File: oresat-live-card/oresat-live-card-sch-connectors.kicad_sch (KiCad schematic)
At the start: 14 parts, among them J1 ORESAT-DEBUG-CONNECTOR, J4 TFM-120-01-L-D-RA, J6 SMPM, J8 SMPM

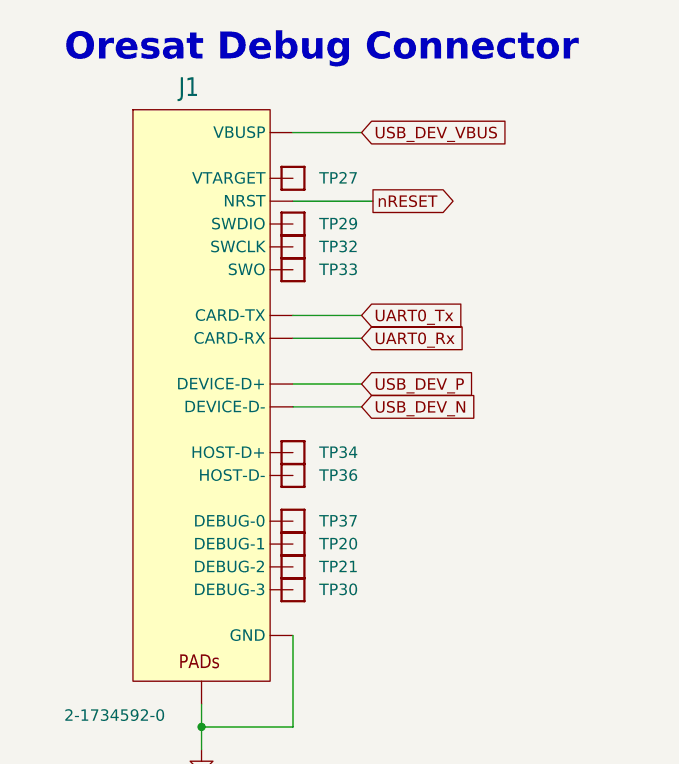
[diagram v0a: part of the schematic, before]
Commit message: Updated OPD / power page and synced with CFC processor, fixed layout issues.
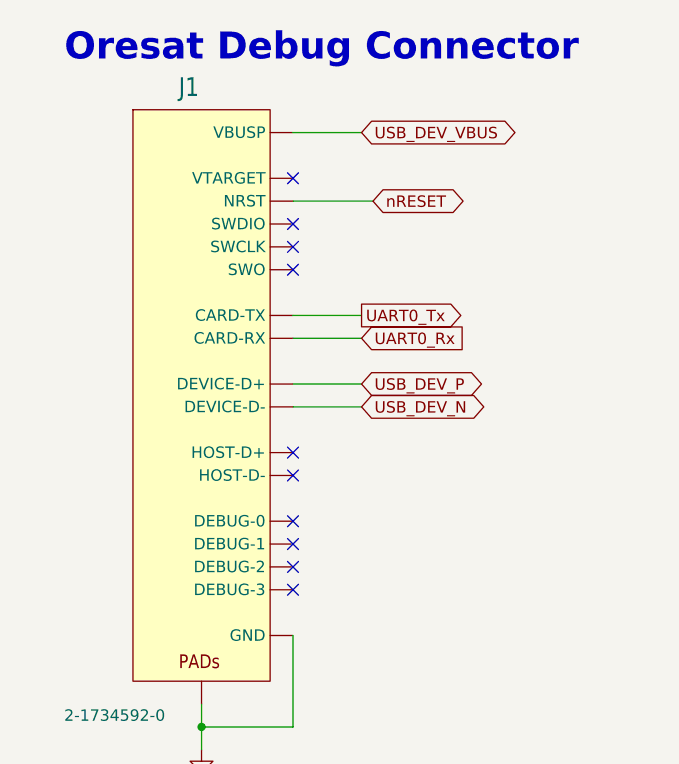
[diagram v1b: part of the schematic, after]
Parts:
- removed TP20, TP21, TP27, TP29, TP30, TP32, TP33, TP34, TP36, TP37: TEST-POINT, oresat-misc:TestPoint_Pad_D1.0mm, symbol oresat-misc:Test-Point-1mm-round
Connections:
- no-connect marks 20 -> 30

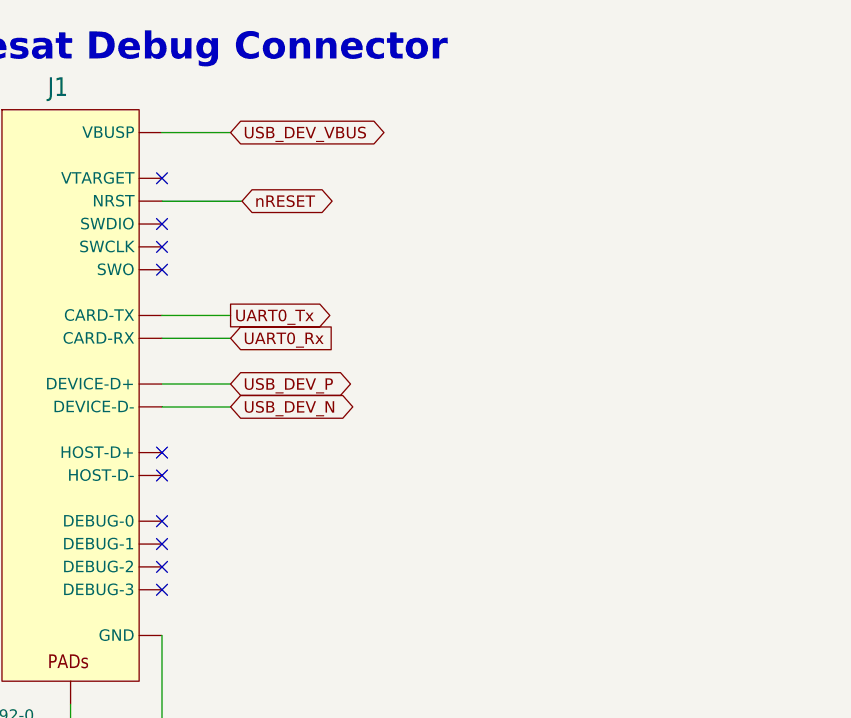
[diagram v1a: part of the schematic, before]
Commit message: Updated SIP A, B, and C. Lots of cleanup of crazy routing - this board is long in the tooth and has been rerouted several times, so there's a lot of crazy routing. Cleaning up a bit is really helping.
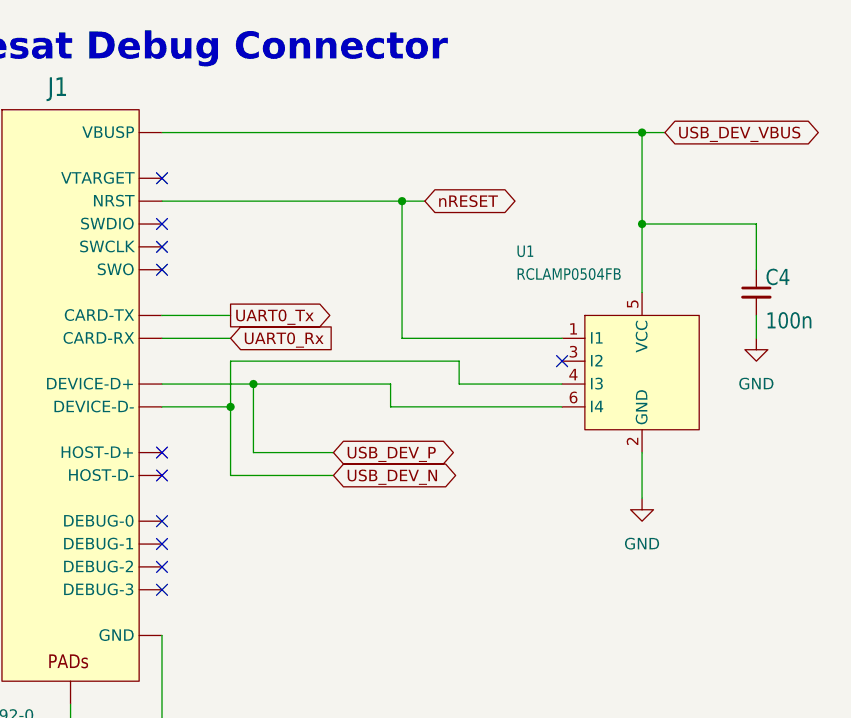
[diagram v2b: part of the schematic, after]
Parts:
- added C4: 100n, Resistor_SMD:R_0603_1608Metric, symbol Device:C_Small
- added U1: RCLAMP0504FB, oresat-live-card:SC70-6, symbol oresat-ics:RCLAMP0504FB
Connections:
- net GND: now also C4.2, U1.2 (GND)
- net USB_DEV_N: now also U1.4 (I3)
- net USB_DEV_P: now also U1.6 (I4)
- net USB_DEV_VBUS: now also C4.1, U1.5 (VCC)
- net nRESET: now also U1.1 (I1)
- no-connect marks 30 -> 31

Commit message: added Olivers BOM and footprint changes, cleaned up pcb
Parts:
- C4: footprint Resistor_SMD:R_0603_1608Metric -> oresat-passives:0603-C
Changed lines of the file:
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@@
 			)
 		)
-		(property "Footprint" "Resistor_SMD:R_0603_1608Metric"
+		(property "Footprint" "oresat-passives:0603-C"
 			(at 353.06 93.98 0)
 			(effects

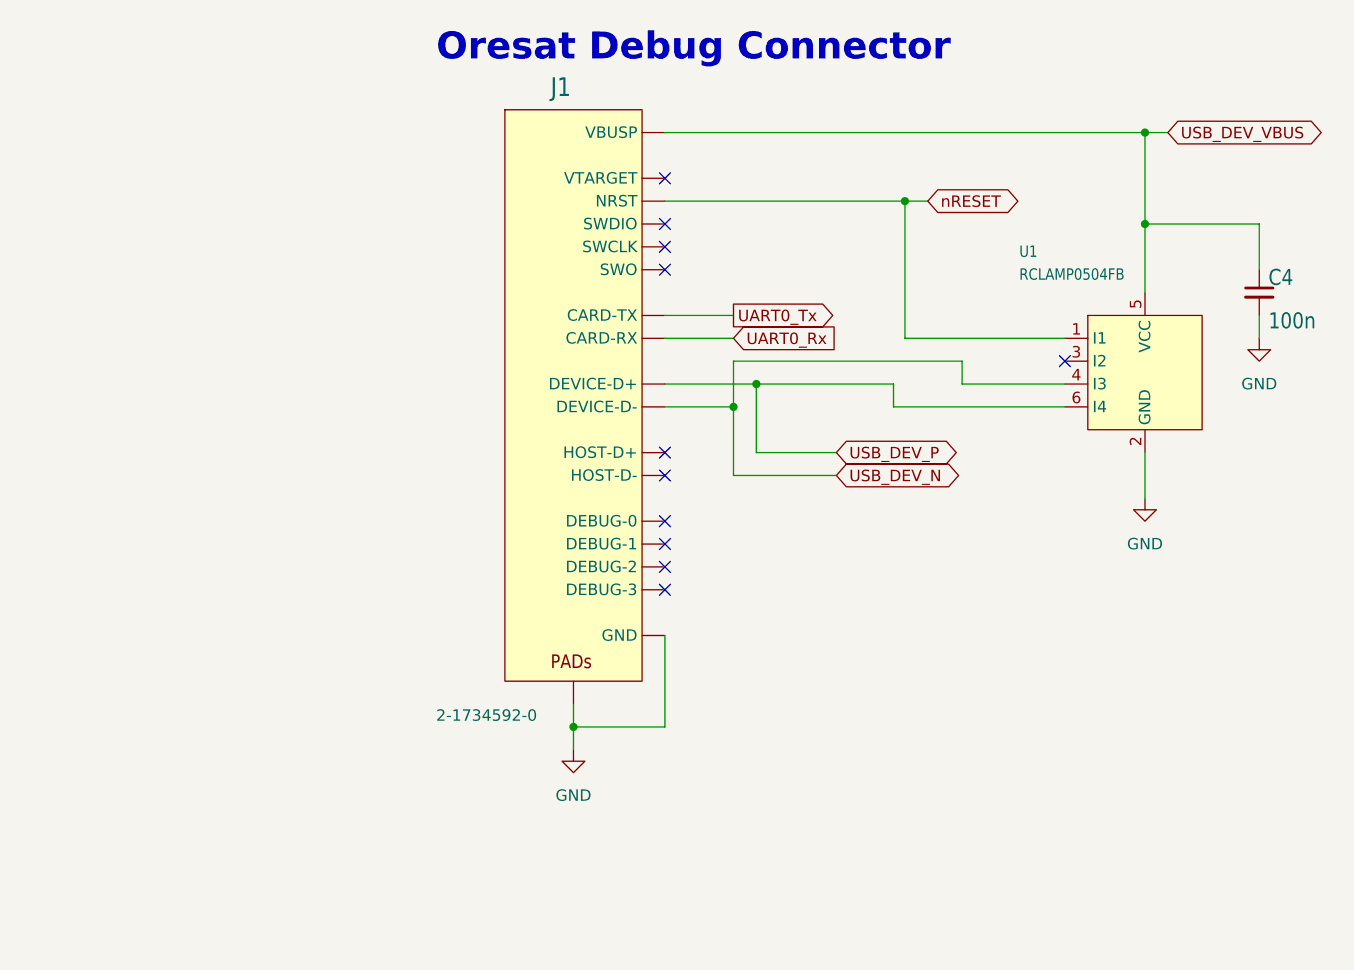
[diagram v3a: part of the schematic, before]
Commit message: Components Update
Changed Debug connector and performed minor rerouting
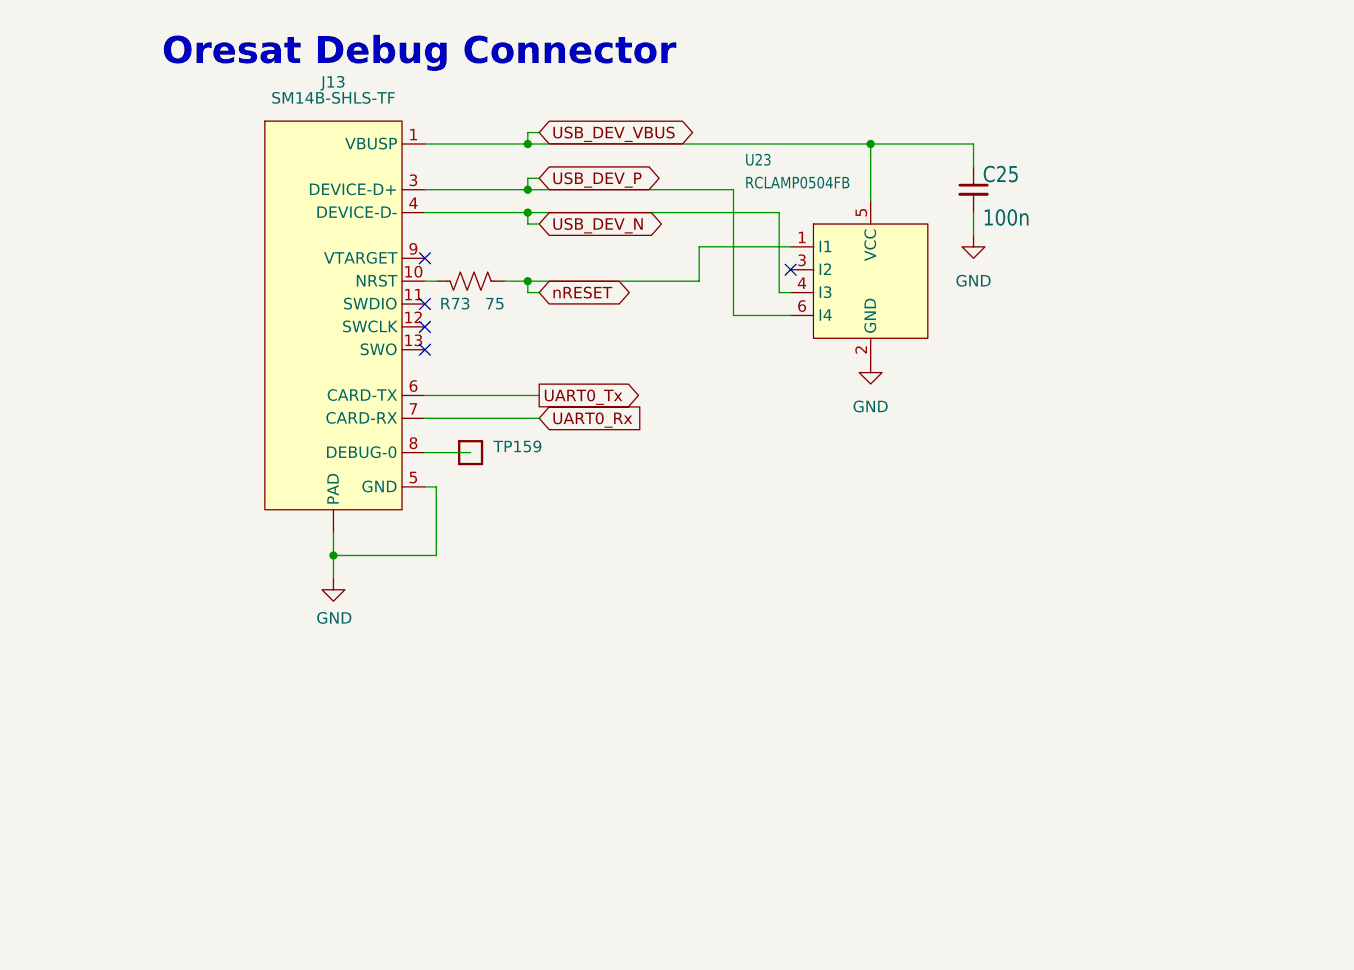
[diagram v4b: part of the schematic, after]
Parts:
- removed C4: 100n, oresat-passives:0603-C, symbol Device:C_Small
- removed J1: ORESAT-DEBUG-CONNECTOR, oresat-connectors:J-TE-2-1734592-0, symbol oresat-connectors:J-TE-2-1734592-0
- removed U1: RCLAMP0504FB, oresat-live-card:SC70-6, symbol oresat-ics:RCLAMP0504FB
- added C25: 100n, oresat-passives:0603-C, symbol Device:C_Small
- added J13: SM14B-SHLS-TF, oresat-connectors:J-JST-SM14BSHLSTF, symbol oresat-connectors:ORESAT-DEBUG-CONNECTOR-3
- added R73: 75, Resistor_SMD:R_0603_1608Metric, symbol Device:R_US
- added TP159: 0.03x0.04, oresat-misc:TestPoint-0.75mm-th, symbol oresat-misc:Test-Point-1mm-round
- added U23: RCLAMP0504FB, oresat-live-card:SC70-6, symbol oresat-ics:RCLAMP0504FB
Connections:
- net GND: now also C25.2, J13.14 (GND), J13.15 (PAD), J13.16 (PAD), J13.5 (GND), U23.2 (GND)
- net UART0_Rx: now also J13.7 (CARD-RX)
- net UART0_Tx: now also J13.6 (CARD-TX)
- net USB_DEV_N: now also J13.4 (DEVICE-D-), U23.4 (I3)
- net USB_DEV_P: now also J13.3 (DEVICE-D+), U23.6 (I4)
- net USB_DEV_VBUS: now also C25.1, J13.1 (VBUSP), J13.2 (VBUSP), U23.5 (VCC)
- net nRESET: now also R73.2, U23.1 (I1)
- new net: J13.10 (NRST), R73.1
- new net: J13.8 (DEBUG-0), TP159.1
- no-connect marks 31 -> 25

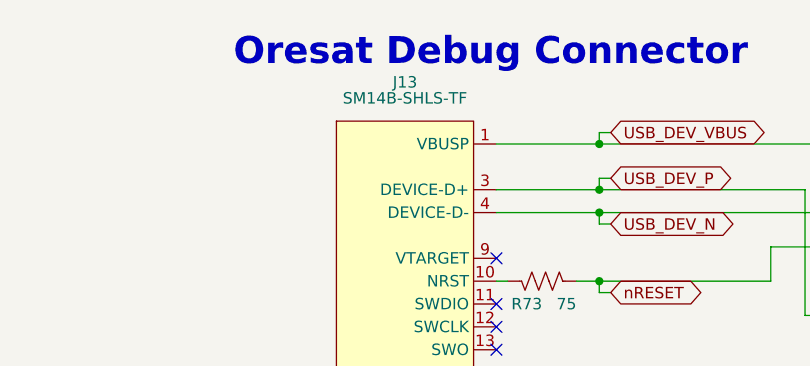
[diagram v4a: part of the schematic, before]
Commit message: Updates to J1 and J5
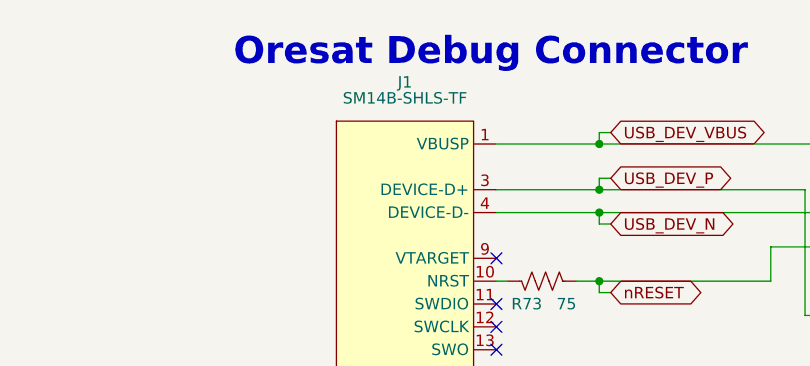
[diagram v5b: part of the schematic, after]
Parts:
- renumbered J13 to J1
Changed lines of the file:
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@@
 		(in_pos_files yes)
 		(dnp no)
-		(property "Reference" "J13"
+		(property "Reference" "J1"
 			(at 250.19 70.612 0)
 			(show_name no)
@@
 			(project "oresat-live-card"
 				(path "/748bdd2d-da0a-4240-ba60-0bf881d2ec56/1bdb8d5b-8060-49dd-b753-8985e7684076"
-					(reference "J13")
+					(reference "J1")
 					(unit 1)
 				)
